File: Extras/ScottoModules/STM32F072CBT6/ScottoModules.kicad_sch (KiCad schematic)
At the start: 18 parts, among them J1 USB_C, SW1 SW_Push, U1 STM32F072CBT6, U3 XC6206, U4 USBLC6-2SC6

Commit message: Added MPN
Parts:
- C1, C2, C3, C4, C5, C7: MPN (none) -> CL05B104KB54PNC
- C6: MPN (none) -> CL10A106KP8NNNC
- C8, C9: MPN (none) -> CL05A105KA5NQNC
- F1: MPN (none) -> MF-FSMF050X-2
- J1: MPN (none) -> TYPE-C-31-M-12
- R1: MPN (none) -> 0402WGF1002TCE
- R2, R3: MPN (none) -> 0402WGF5101TCE
- SW1: MPN (none) -> SKQGABE010
- U1: MPN (none) -> STM32F072CBT6
- U3: MPN (none) -> XC6206P332MR-G
- U4: MPN (none) -> USBLC6-2SC6
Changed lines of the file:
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@@
+			)
+		)
+		(property "MPN" "STM32F072CBT6"
+			(at 46.99 207.01 0)
+			(effects
+				(font
+					(size 1.27 1.27)
+				)
+				(hide yes)
 			)
 		)
@@
 		)
 		(property "JlcRotOffset" "180"
+			(at 236.22 265.43 0)
+			(effects
+				(font
+					(size 1.27 1.27)
+				)
+				(hide yes)
+			)
+		)
+		(property "MPN" "XC6206P332MR-G"
 			(at 236.22 265.43 0)
 			(effects
@@
 			)
 		)
+		(property "MPN" "CL10A106KP8NNNC"
+			(at 82.55 269.24 0)
+			(effects
+				(font
+					(size 1.27 1.27)
+				)
+				(hide yes)
+			)
+		)
 		(pin "1"
 		)
@@
 			)
 		)
+		(property "MPN" "0402WGF1002TCE"
+			(at 107.95 243.84 0)
+			(effects
+				(font
+					(size 1.27 1.27)
+				)
+				(hide yes)
+			)
+		)
 		(pin "2"
 		)
@@
 			)
 		)
+		(property "MPN" "USBLC6-2SC6"
+			(at 195.58 257.81 0)
+			(effects
+				(font
+					(size 1.27 1.27)
+				)
+				(hide yes)
+			)
+		)
 		(pin "6"
 		)
@@
 			)
 		)
+		(property "MPN" "CL05A105KA5NQNC"
+			(at 227.33 267.97 0)
+			(effects
+				(font
+					(size 1.27 1.27)
+				)
+				(hide yes)
+			)
+		)
 		(pin "1"
 		)
@@
 			)
 		)
+		(property "MPN" "CL05B104KB54PNC"
+			(at 59.69 269.24 0)
+			(effects
+				(font
+					(size 1.27 1.27)
+				)
+				(hide yes)
+			)
+		)
 		(pin "1"
 		)
@@
 			)
 		)
+		(property "MPN" "CL05B104KB54PNC"
+			(at 36.83 269.24 0)
+			(effects
+				(font
+					(size 1.27 1.27)
+				)
+				(hide yes)
+			)
+		)
 		(pin "1"
 		)
@@
 			)
 		)
+		(property "MPN" "CL05B104KB54PNC"
+			(at 27.94 171.45 0)
+			(effects
+				(font
+					(size 1.27 1.27)
+				)
+				(hide yes)
+			)
+		)
 		(pin "2"
 		)
@@
 		(property "LCSC" "C25905"
 			(at 158.75 240.03 90)
+			(effects
+				(font
+					(size 1.27 1.27)
+				)
+				(hide yes)
+			)
+		)
+		(property "MPN" "0402WGF5101TCE"
+			(at 158.75 240.03 0)
 			(effects
 				(font
@@
 			)
 		)
+		(property "MPN" "0402WGF5101TCE"
+			(at 158.75 237.49 0)
+			(effects
+				(font
+					(size 1.27 1.27)
+				)
+				(hide yes)
+			)
+		)
 		(pin "2"
 		)
@@
 			)
 		)
+		(property "MPN" "CL05B104KB54PNC"
+			(at 48.26 269.24 0)
+			(effects
+				(font
+					(size 1.27 1.27)
+				)
+				(hide yes)
+			)
+		)
 		(pin "1"
 		)
@@
 			)
 		)
+		(property "MPN" "MF-FSMF050X-2"
+			(at 162.56 232.41 0)
+			(effects
+				(font
+					(size 1.27 1.27)
+				)
+				(hide yes)
+			)
+		)
 		(pin "1"
 		)
@@
 			)
 		)
+		(property "MPN" "TYPE-C-31-M-12"
+			(at 139.7 247.65 0)
+			(effects
+				(font
+					(size 1.27 1.27)
+				)
+				(hide yes)
+			)
+		)
 		(pin "A12"
 		)
@@
 			)
 		)
+		(property "MPN" "CL05B104KB54PNC"
+			(at 25.4 269.24 0)
+			(effects
+				(font
+					(size 1.27 1.27)
+				)
+				(hide yes)
+			)
+		)
 		(pin "1"
 		)
@@
 		)
 		(property "LCSC" "C115351"
+			(at 97.79 243.84 0)
+			(effects
+				(font
+					(size 1.27 1.27)
+				)
+				(hide yes)
+			)
+		)
+		(property "MPN" "SKQGABE010"
 			(at 97.79 243.84 0)
 			(effects
@@
 			)
 		)
+		(property "MPN" "CL05A105KA5NQNC"
+			(at 245.11 267.97 0)
+			(effects
+				(font
+					(size 1.27 1.27)
+				)
+				(hide yes)
+			)
+		)
 		(pin "1"
 		)
@@
 			(at 71.12 269.24 0)
 			(effects
+				(font
+					(size 1.27 1.27)
+				)
+				(hide yes)
+			)
+		)
+		(property "MPN" "CL05B104KB54PNC"
+			(at 71.12 269.24 0)
+			(effects

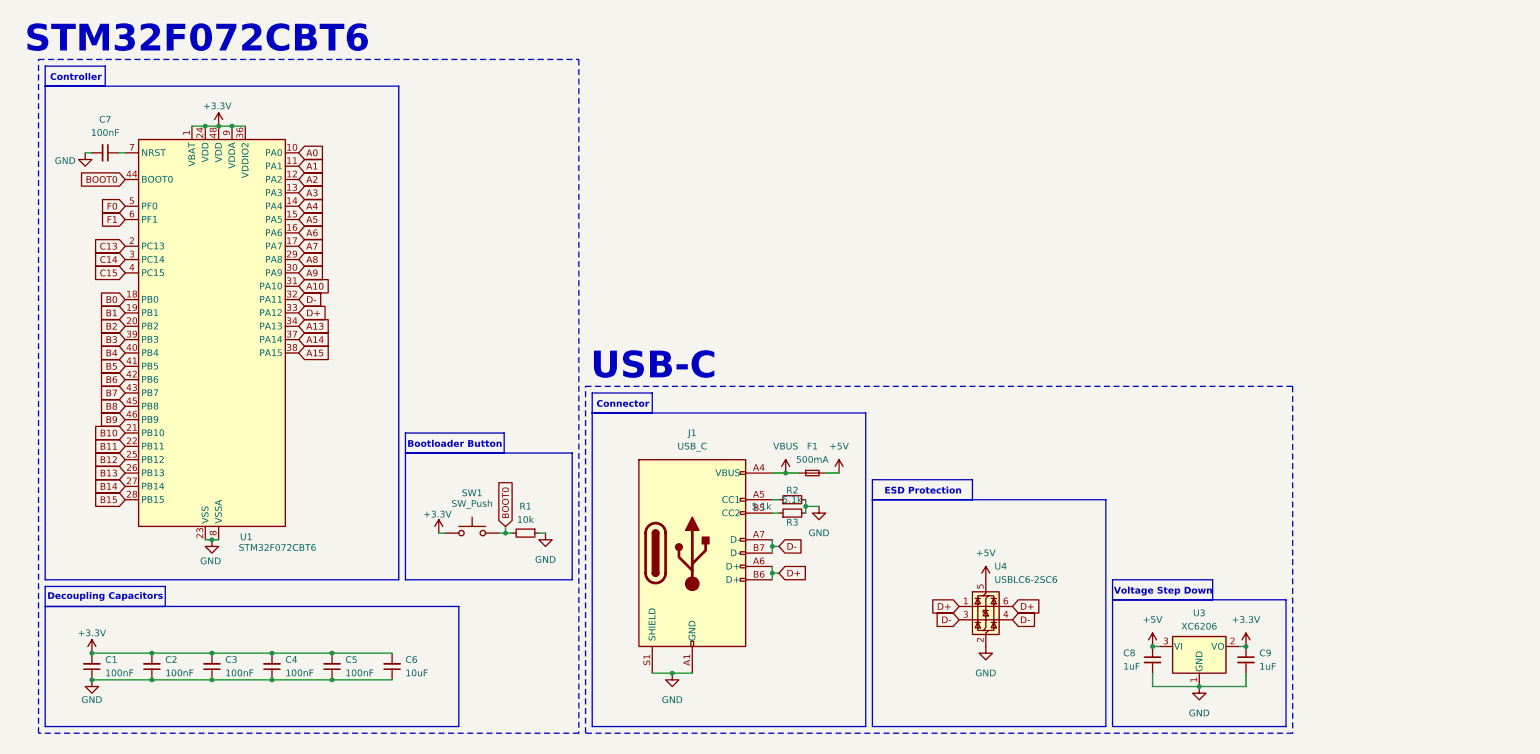
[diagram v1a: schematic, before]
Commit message: Added Power Flags
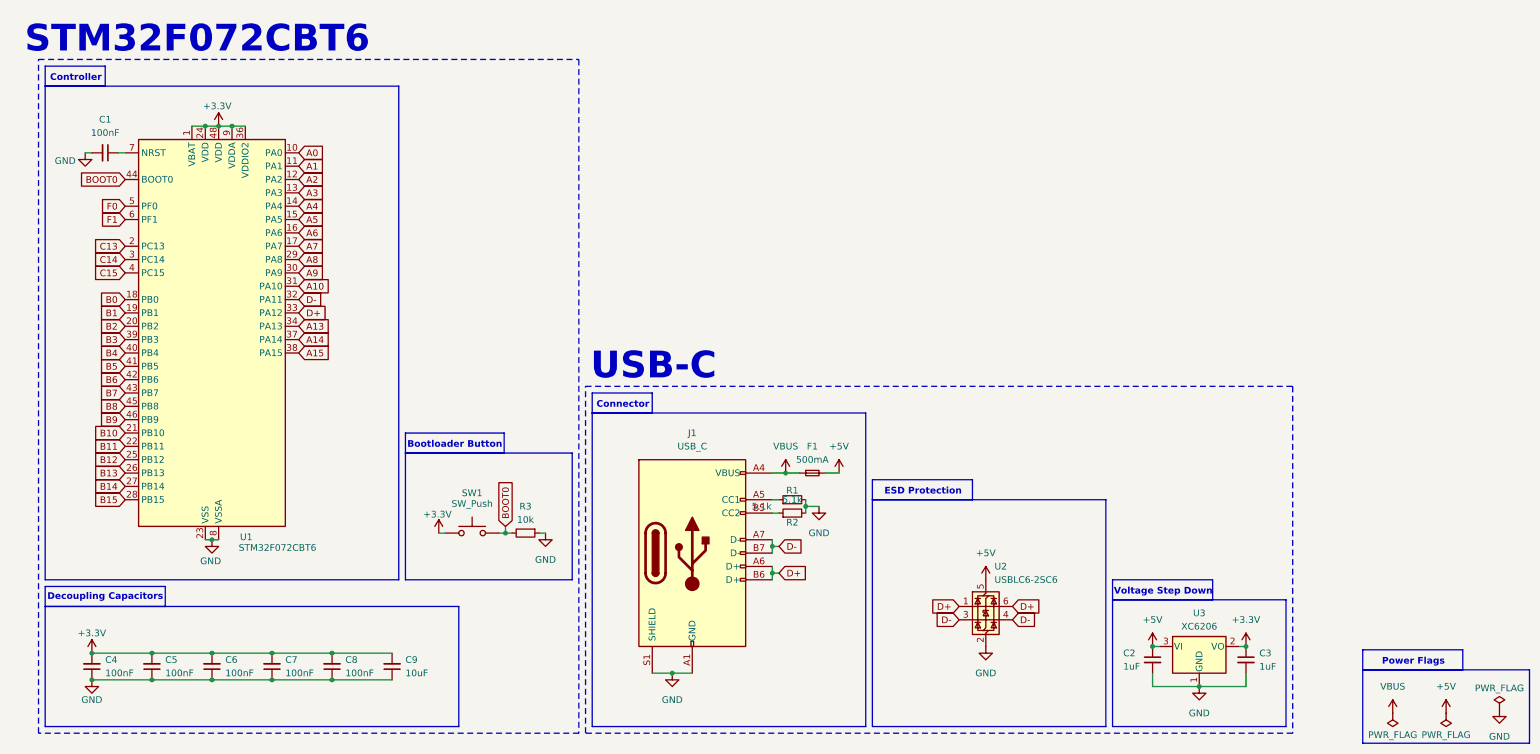
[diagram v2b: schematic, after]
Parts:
- renumbered C7 to C1, C8 to C2, C9 to C3, C1 to C4, C2 to C5, C3 to C6, C4 to C7, C5 to C8, C6 to C9, R2 to R1, R3 to R2, R1 to R3, U4 to U2
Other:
- note added: "Power Flags"

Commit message: Modified PCB Project
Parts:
- removed J1: USB_C, ScottoKeebs_Components:USB_C_HRO_TYPE-C-31-M-12, symbol Connector:USB_C_Receptacle_USB2.0_14P
- added C10: 100nF, Capacitor_SMD:C_0402_1005Metric, symbol Device:C_Small
- added C11: 4.7uF, Capacitor_SMD:C_0402_1005Metric, symbol Device:C_Small
- added J1: USB_C_Receptacle_USB2.0_16P, Connector_USB:USB_C_Receptacle_HRO_TYPE-C-31-M-12, symbol Connector:USB_C_Receptacle_USB2.0_16P
- C1, C4, C5, C7: footprint ScottoKeebs_Components:Capacitor_0402 -> Capacitor_SMD:C_0402_1005Metric
- C2, C3: footprint ScottoKeebs_Components:Capacitor_0402 -> Capacitor_SMD:C_0603_1608Metric; LCSC C52923 -> C15849; MPN CL05A105KA5NQNC -> CL10A105KB8NNNC
- C6: value 100nF -> 4.7uF; footprint ScottoKeebs_Components:Capacitor_0402 -> Capacitor_SMD:C_0402_1005Metric; LCSC C307331 -> C23733; MPN CL05B104KB54PNC -> CL05A475MP5NRNC
- C8: value 100nF -> 10nF; footprint ScottoKeebs_Components:Capacitor_0402 -> Capacitor_SMD:C_0402_1005Metric; LCSC C307331 -> C15195; MPN CL05B104KB54PNC -> CL05B103KB5NNNC
- C9: value 10uF -> 1uF; footprint ScottoKeebs_Components:Capacitor_0603 -> Capacitor_SMD:C_0402_1005Metric; LCSC C19702 -> C52923; MPN CL10A106KP8NNNC -> CL05A105KA5NQNC
- F1: footprint ScottoKeebs_Components:Fuse_0603 -> Fuse:Fuse_0603_1608Metric
- R1, R2, R3: footprint ScottoKeebs_Components:Resistor_0402 -> Resistor_SMD:R_0402_1005Metric
- SW1: footprint ScottoKeebs_Components:Button_TL3342 -> Button_Switch_SMD:SW_SPST_TL3342
- U1: footprint ScottoKeebs_Components:Package_LQFP-48_7x7mm_P0.5 -> Package_QFP:LQFP-48_7x7mm_P0.5mm
- U2: footprint ScottoKeebs_Components:ESD_SOT-23-6 -> Package_TO_SOT_SMD:SOT-23-6; JlcRotOffset -90 -> (none); LCSC C2827654 -> (none); MPN USBLC6-2SC6 -> (none)
- U3: value XC6206 -> XC6206PxxxMR; footprint ScottoKeebs_Components:Voltage_SOT-23 -> Package_TO_SOT_SMD:SOT-23-3
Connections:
- net +3.3V: now also C3.2, C10.2, C11.2; no longer C3.1
- net +5V: now also C2.2; no longer C2.1, U2.5 (VBUS)
- net GND: now also C2.1, C3.1, C10.1, C11.1, J1.A1 (GND), J1.A12 (GND), J1.B1 (GND), J1.B12 (GND), J1.S1 (SHIELD); no longer C2.2, C3.2
- net VBUS: now also U2.5 (VBUS), J1.A4 (VBUS), J1.A9 (VBUS), J1.B4 (VBUS), J1.B9 (VBUS)
- net NRST: now reaches C1.1, U1.7 (NRST)
- net at R2.1: now also J1.B5 (CC2)
- net at R1.1: now also J1.A5 (CC1)
- net D+ renamed MCU-D+
- net MCU-D+: no longer U2.6 (I/O1)
- net D- renamed MCU-D-
- net MCU-D-: no longer U2.4 (I/O2)
- new net USB-D+: J1.A6 (D+), J1.B6 (D+), U2.6 (I/O1)
- new net USB-D-: J1.A7 (D-), J1.B7 (D-), U2.4 (I/O2)
- no-connect marks 0 -> 2
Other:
- note added: "Keep pressed while pluggin in the board to enter DFU"
- moved on the sheet: C1
